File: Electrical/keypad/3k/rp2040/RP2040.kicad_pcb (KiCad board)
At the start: 4 copper layers, 66.7 x 67.2 mm, 73 parts, among them J1 Conn_01x04_Socket, P1 USB-TYPE-C-016, Q1 BSS138, SW1 TS-1187A-B-A-B, SW2 TS-1187A-B-A-B, SW3 BUTT1, SW4 BUTT2, SW5 BUTT3, U1 PRTR5V0U2X, U3 RP2040, U5 W25Q16JVSS, U6 ME6212C33M5G, U7 SLSS49E, U8 SLSS49E, U9 SLSS49E, Y1 12MHz

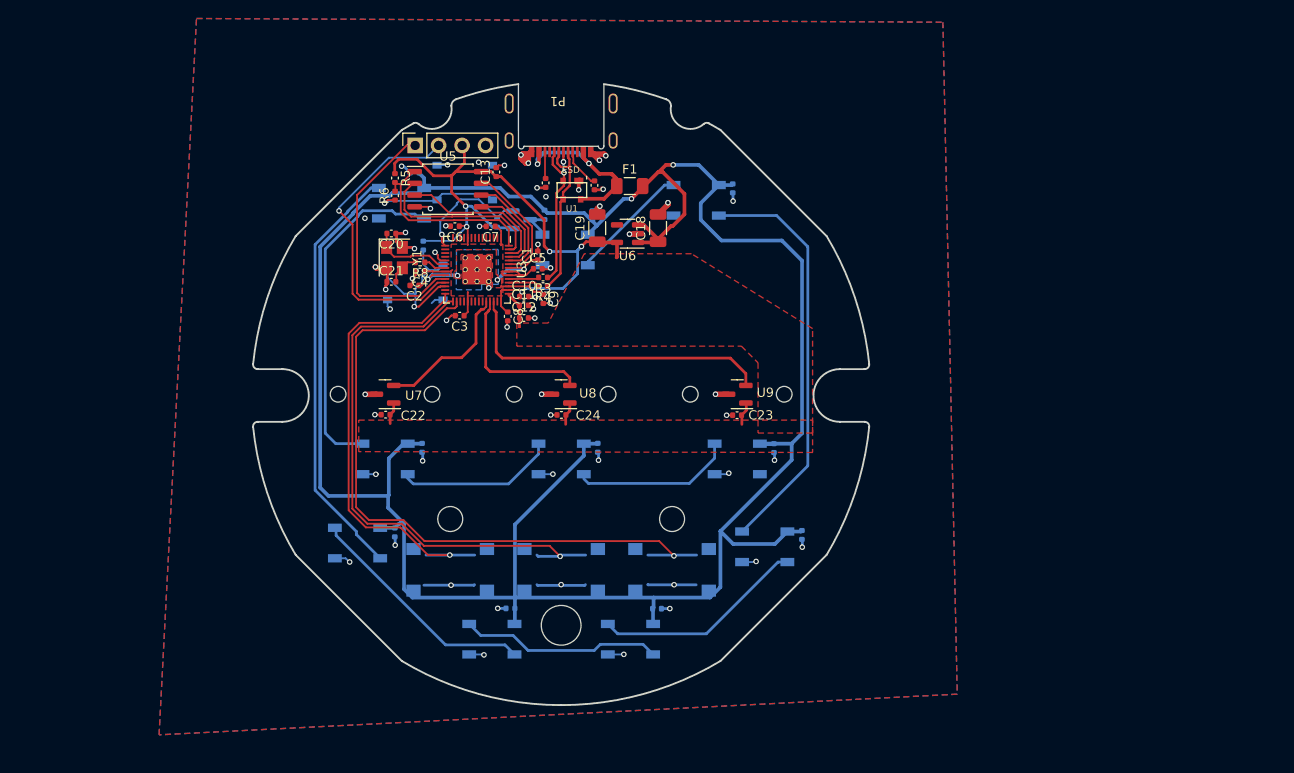
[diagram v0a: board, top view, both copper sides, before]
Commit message: adds all circuit components needed for final pcb, but may need more LED
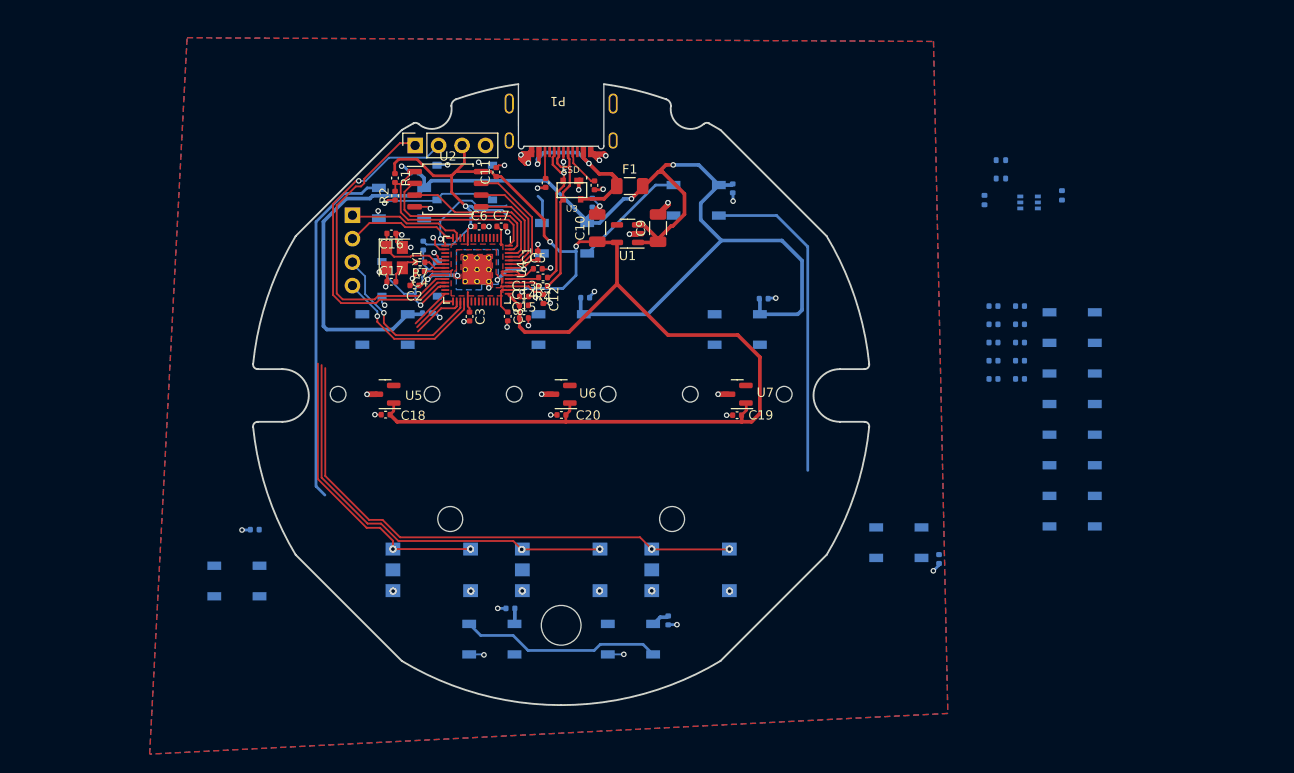
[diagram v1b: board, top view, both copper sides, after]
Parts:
- removed Q1: BSS138, Package_TO_SOT_SMD:SOT-23
- removed the SW4 at (100.0, 119.0)
- removed the SW5 at (112.0, 119.0)
- added C21: 100n, Capacitor_SMD:C_0402_1005Metric, B.Cu at (149.6, 90.5)
- added C22: 100n, Capacitor_SMD:C_0402_1005Metric, B.Cu at (149.6, 92.4)
- added C23: 100n, Capacitor_SMD:C_0402_1005Metric, B.Cu at (149.6, 94.4)
- added C31: 100n, Capacitor_SMD:C_0402_1005Metric, B.Cu at (149.6, 96.4)
- added C32: 100n, Capacitor_SMD:C_0402_1005Metric, B.Cu at (149.6, 98.3)
- added C33: 100n, Capacitor_SMD:C_0402_1005Metric, B.Cu at (146.8, 90.5)
- added C34: 100n, Capacitor_SMD:C_0402_1005Metric, B.Cu at (146.8, 92.4)
- added D10: WS2812B, LED_SMD:LED_WS2812B_PLCC4_5.0x5.0mm_P3.2mm, B.Cu at (155.3, 106.0)
- added D11: WS2812B, LED_SMD:LED_WS2812B_PLCC4_5.0x5.0mm_P3.2mm, B.Cu at (155.3, 112.7)
- added D8: WS2812B, LED_SMD:LED_WS2812B_PLCC4_5.0x5.0mm_P3.2mm, B.Cu at (155.3, 92.8)
- added D9: WS2812B, LED_SMD:LED_WS2812B_PLCC4_5.0x5.0mm_P3.2mm, B.Cu at (155.3, 99.4)
- added J1: Conn_01x04_Socket, Connector_PinSocket_2.54mm:PinSocket_1x04_P2.54mm_Vertical, B.Cu at (77.4, 80.6)
- added R10: 5.1k, Capacitor_SMD:C_0402_1005Metric, B.Cu at (146.8, 96.4)
- added R11: 5.1k, Capacitor_SMD:C_0402_1005Metric, B.Cu at (146.8, 98.3)
- added R14: 10k, Resistor_SMD:R_0402_1005Metric, B.Cu at (147.6, 74.7)
- added R15: 10k, Resistor_SMD:R_0402_1005Metric, B.Cu at (147.6, 76.7)
- added R9: 5.1k, Capacitor_SMD:C_0402_1005Metric, B.Cu at (146.8, 94.4)
- added SW1: KAN0644-0551B1-A, push_button_keypad:KAN0644, B.Cu at (86.0, 119.0)
- added SW2: KAN0644-0551B1-A, push_button_keypad:KAN0644, B.Cu at (100.0, 119.0)
- added T1: BSS138BKS_115, Package_TO_SOT_SMD:SOT-363_SC-70-6, B.Cu at (150.6, 79.2)
- SW3: value BUTT1 -> KAN0644-0551B1-A; footprint Button_Switch_SMD:SW_Push_1P1T_NO_6x6mm_H9.5mm -> push_button_keypad:KAN0644
- moved R13 56.0 mm to (154.2, 78.5)
- moved R12 52.8 mm to (145.8, 79.0)
- moved SW3 26.0 mm to (114.0, 119.0)
- moved C36 16.3 mm to (102.6, 89.6), turned to 0 degrees
- moved C37 16.2 mm to (121.9, 89.7), turned to 0 degrees
- moved C29 15.2 mm to (66.8, 114.7), turned to 180 degrees
- moved C26 15.1 mm to (140.9, 117.8)
- moved C35 14.6 mm to (85.5, 91.2), turned to 0 degrees
- moved D3 14.5 mm to (136.5, 116.1)
- moved D12 14.0 mm to (81.0, 93.0)
- moved D13 14.0 mm to (100.0, 93.0)
- moved D14 14.0 mm to (119.0, 93.0)
- moved D6 13.7 mm to (64.9, 120.2)
- moved C6 2.63 mm to (91.1, 81.9), turned to 0 degrees
- moved C27 1.75 mm to (111.6, 124.5), turned to -90 degrees
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- renumbered C19 to C10, C13 to C11, C9 to C12, C10 to C13, C11 to C14, C12 to C15, C20 to C16, C21 to C17, C22 to C18, C23 to C19, C24 to C20, C28 to C24, C29 to C25, C30 to C26, C31 to C27, C32 to C28, C33 to C29, C34 to C30, C25 to C35, C26 to C36, C27 to C37, C18 to C9, D4 to D1, D1 to D12, D2 to D13, D3 to D14, D5 to D2, D6 to D3, D7 to D4, D8 to D5, D9 to D6, D10 to D7, J1 to J2, R5 to R1, R9 to R12, R10 to R13, R6 to R2, R1 to R5, R2 to R6, R8 to R7, R7 to R8, SW1 to SW4, SW2 to SW5, U6 to U1, U5 to U2, U1 to U3, U3 to U4, U7 to U5, U8 to U6, U9 to U7
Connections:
- net LED_D renamed U_LED_D
- D12 pad 4: BL_DIN -> Net-(D12-DIN)
- D7 pad 2: BL_DIN -> Net-(D7-DOUT)
- SW3 pad 1: BUTT0 -> BUTT2
- U4 pad 13: /GPIO10 -> SDA_1
- U4 pad 14: /GPIO11 -> SCL_1
- U4 pad 16: /GPIO13 -> BL_LED_D
- U4 pad 31: /GPIO20 -> SDA_0
- U4 pad 32: /GPIO21 -> SCL_0
- U5 pad 2: ADC_IN1 -> Net-(U5-VOUT)
- U6 pad 2: ADC_IN2 -> Net-(U6-VOUT)
- U7 pad 2: ADC_IN3 -> Net-(U7-VOUT)
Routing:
- net +5V: track 260.4 -> 147.4 mm
- net +3V3: track 99.0 -> 177.0 mm
- net BL_DIN: track 36.8 -> 0.00 mm
- net ADC_IN3: track 34.8 -> 0.00 mm
- net GND: track 85.5 -> 57.7 mm, vias 59 -> 55
- net Net-(D5-DOUT): track 25.3 -> 0.00 mm
- net Net-(D3-DOUT): track 23.1 -> 0.00 mm
- net SDA_0: track 0.00 -> 18.6 mm, vias 0 -> 1
- net ADC_IN2: track 17.7 -> 0.00 mm
- net SCL_0: track 0.00 -> 17.3 mm, vias 0 -> 1
- net Net-(D13-DOUT): track 17.1 -> 0.00 mm
- net Net-(D12-DOUT): track 17.0 -> 0.00 mm
- net ADC_IN1: track 15.8 -> 0.00 mm
- net BUTT0: track 49.9 -> 37.2 mm, vias 1 -> 2
- net SDA_1: track 0.00 -> 12.6 mm
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
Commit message: reverts to using standard bs138 because the dual package one is more expensive than just using two of them, and it's easier to layout
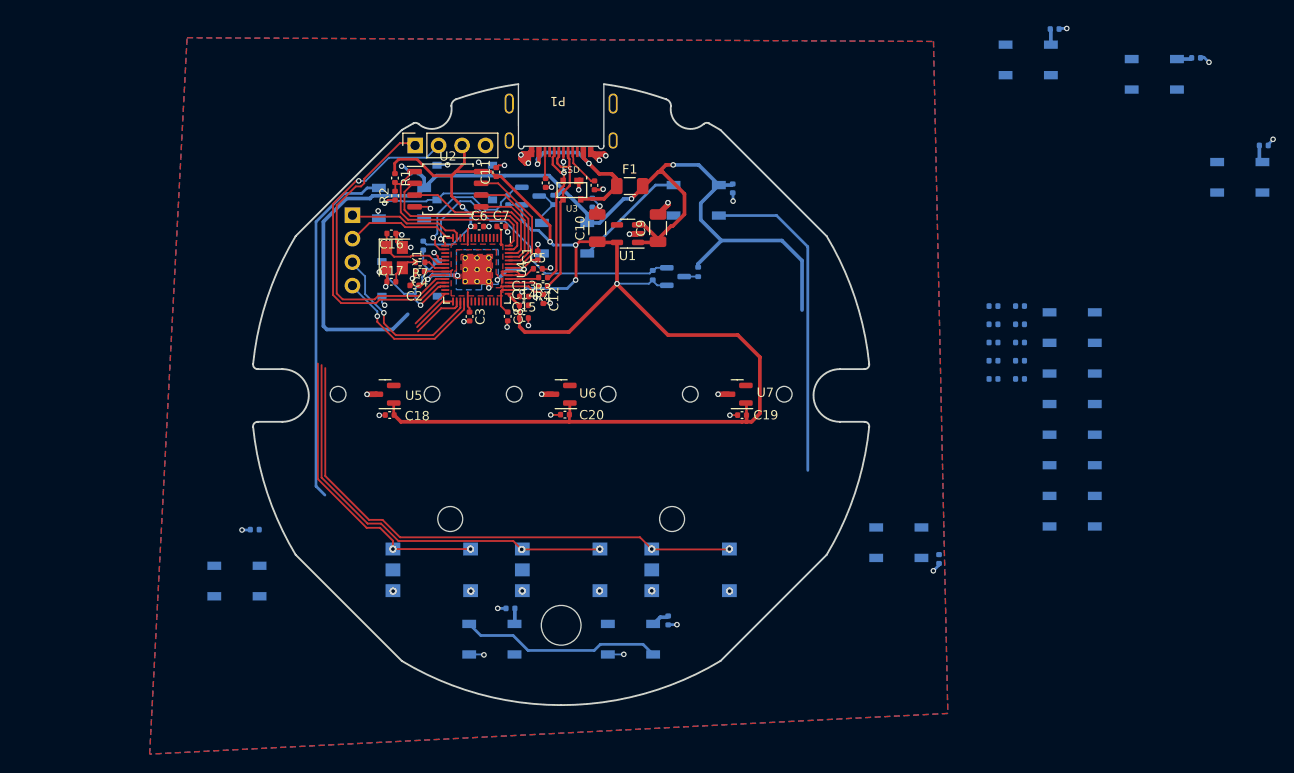
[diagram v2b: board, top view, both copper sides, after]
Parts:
- removed T1: BSS138BKS_115, Package_TO_SOT_SMD:SOT-363_SC-70-6
- added Q1: BSS138, Package_TO_SOT_SMD:SOT-23, B.Cu at (96.7, 78.6)
- added Q2: BSS138, Package_TO_SOT_SMD:SOT-23, B.Cu at (112.4, 87.3)
- moved C35 87.7 mm to (168.7, 63.6)
- moved D12 87.7 mm to (164.2, 65.4)
- moved C36 75.2 mm to (176.0, 73.1)
- moved D13 75.2 mm to (173.4, 76.5)
- moved R13 55.0 mm to (99.1, 79.0)
- moved R12 51.5 mm to (94.3, 79.0)
- moved D14 42.9 mm to (150.5, 63.8)
- moved C37 42.9 mm to (153.4, 60.5)
- moved R14 39.7 mm to (109.9, 87.1), turned to -90 degrees
- moved R15 34.3 mm to (114.8, 86.8), turned to 90 degrees
- moved C19 0.54 mm to (119.6, 102.3)
- moved C18 0.44 mm to (81.5, 102.2)
- moved C20 0.38 mm to (100.4, 102.2)
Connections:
- U4 pad 15: U_LED_D -> BL_LED_D
- U4 pad 16: BL_LED_D -> U_LED_D
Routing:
- net BL_LED_D: track 2.12 -> 32.5 mm
- net +5V: track 147.4 -> 130.7 mm
- net +3V3: track 177.0 -> 183.9 mm, vias 5 -> 7
- net U_LED_D: track 11.2 -> 16.5 mm
- net Net-(D12-DIN): track 0.00 -> 1.56 mm
- net Net-(D1-DIN): track 3.12 -> 4.57 mm

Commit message: places perkey backlight leds
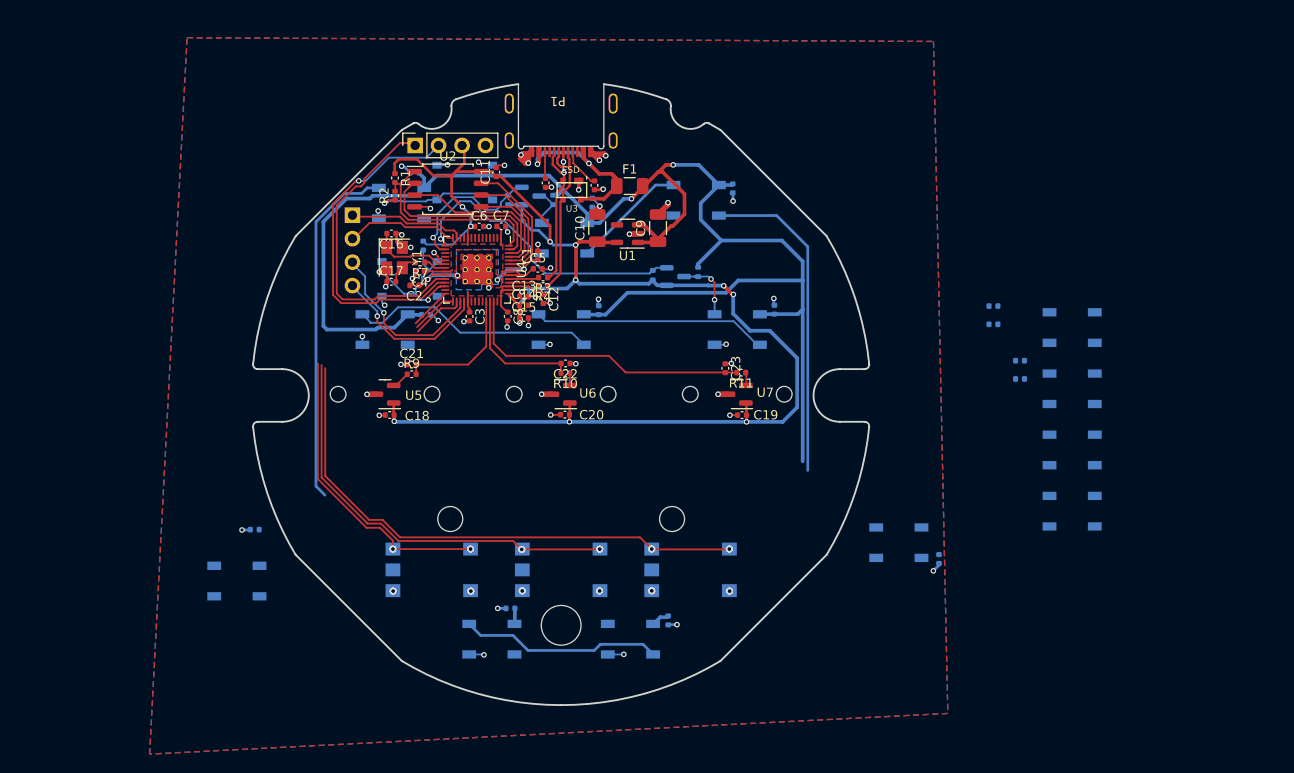
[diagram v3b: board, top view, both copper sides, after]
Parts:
- C21, C22, C23, R10, R11, R9: moved to F.Cu
- moved D14 75.4 mm to (81.0, 93.0)
- moved D13 75.2 mm to (100.0, 93.0)
- moved C37 74.7 mm to (85.4, 91.4)
- moved C36 74.1 mm to (104.1, 90.9), turned to 90 degrees
- moved C21 66.1 mm to (83.8, 96.8), turned to 0 degrees
- moved R9 63.0 mm to (83.8, 97.8), turned to 0 degrees
- moved C35 53.1 mm to (123.1, 90.8), turned to 90 degrees
- moved D12 52.9 mm to (119.0, 93.0)
- moved C22 49.3 mm to (100.5, 96.7)
- moved R10 46.3 mm to (100.5, 97.7)
- moved C23 32.0 mm to (117.8, 97.2), turned to -90 degrees
- moved R11 27.3 mm to (119.5, 97.7)
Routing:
- net +5V: track 130.7 -> 173.4 mm
- net ADC_IN3: track 0.00 -> 32.3 mm
- net Net-(D13-DOUT): track 0.00 -> 26.8 mm
- net Net-(D12-DOUT): track 0.00 -> 25.3 mm
- net ADC_IN2: track 0.00 -> 14.5 mm
- net ADC_IN1: track 0.00 -> 14.3 mm
- net Net-(D12-DIN): track 1.56 -> 7.41 mm, vias 0 -> 2
- net GND: track 57.9 -> 63.8 mm, vias 55 -> 61
- net +3V3: track 183.9 -> 178.2 mm, vias 7 -> 12
- net Net-(U5-VOUT): track 0.00 -> 1.96 mm
- net Net-(U7-VOUT): track 0.00 -> 1.44 mm
- net Net-(U6-VOUT): track 0.00 -> 1.43 mm
- net Net-(U4-RUN): track 17.6 -> 16.9 mm

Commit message: adds buttons
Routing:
- net BUTT1: track 50.5 -> 67.0 mm, vias 2 -> 3
- net BUTT2: track 64.5 -> 80.9 mm, vias 2 -> 3
- net BUTT0: track 37.2 -> 53.5 mm, vias 2 -> 3

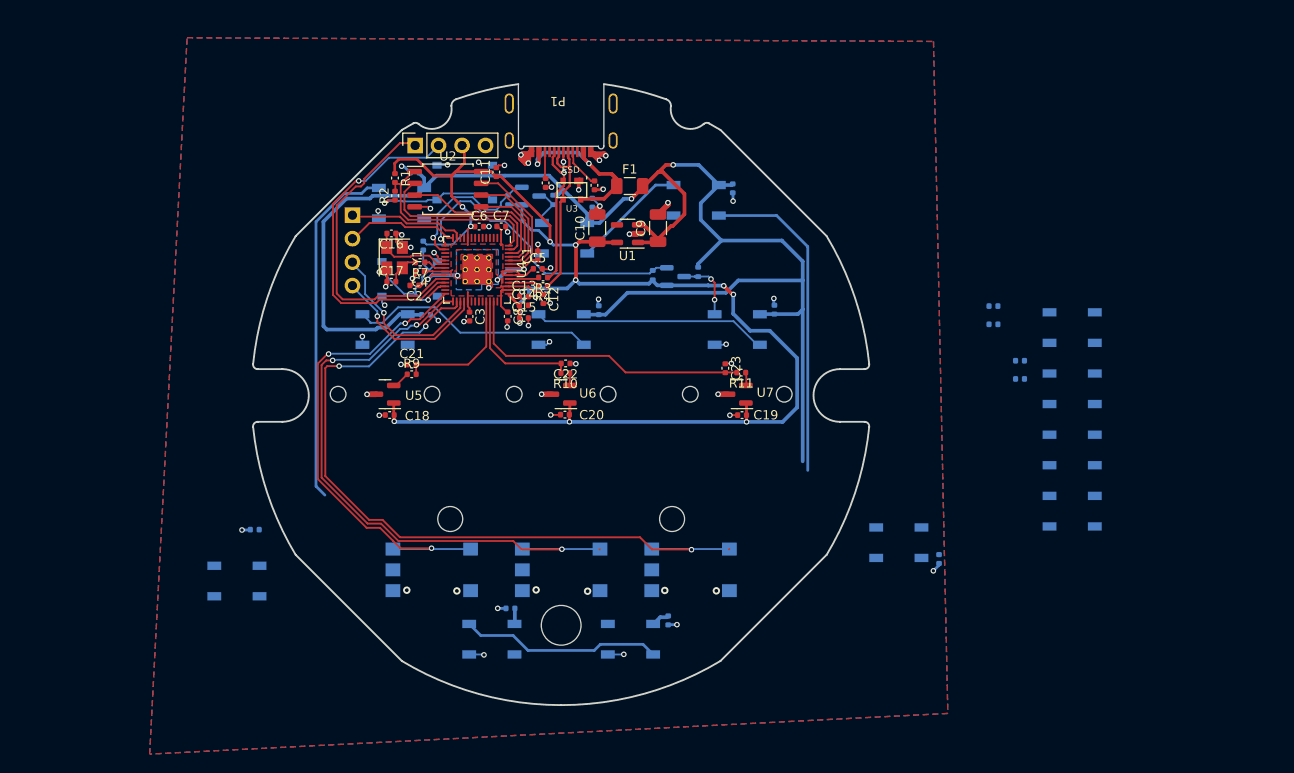
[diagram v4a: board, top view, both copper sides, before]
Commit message: adds 2020 led to smoothen out LED diffusing on sides
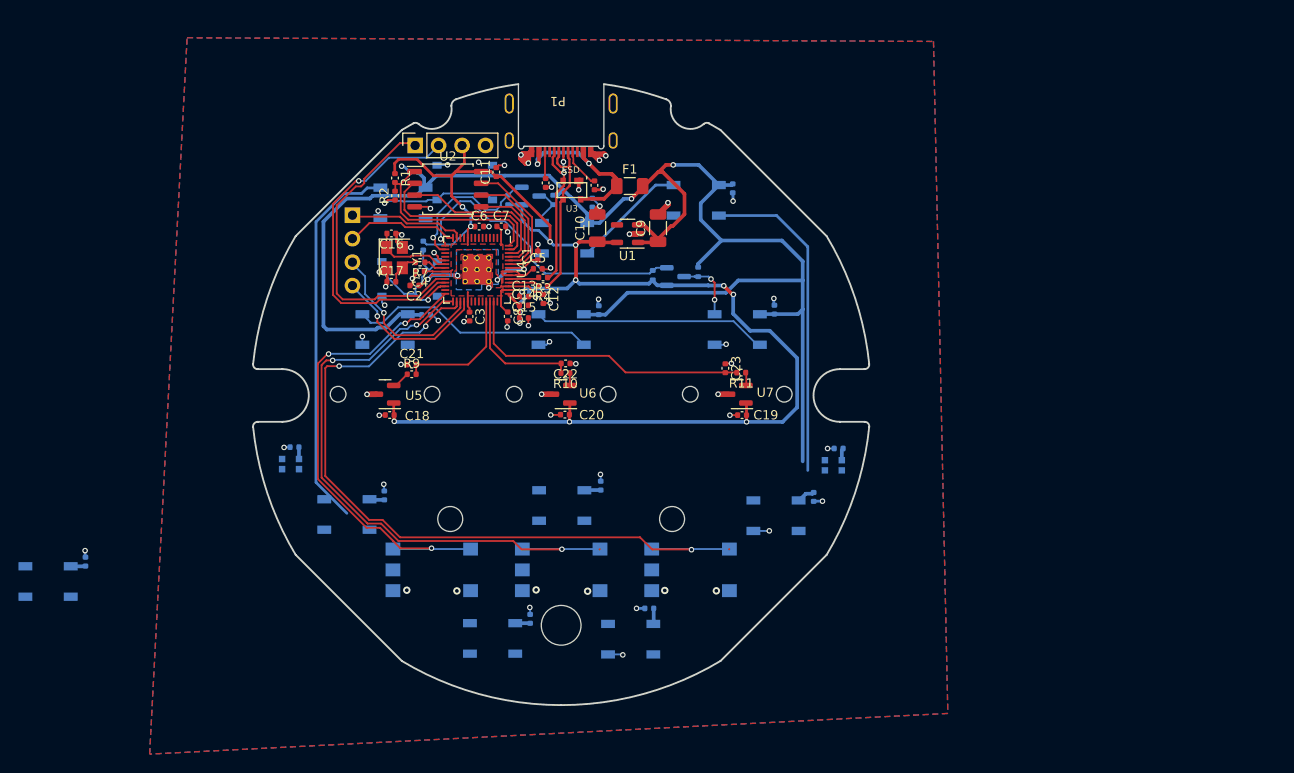
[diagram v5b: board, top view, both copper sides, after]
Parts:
- D10, D3: value WS2812B -> WS2812-2020; footprint LED_SMD:LED_WS2812B_PLCC4_5.0x5.0mm_P3.2mm -> footprints:LED_WS2812-2020
- moved D9 112.7 mm to (44.5, 120.3)
- moved D10 84.6 mm to (70.7, 107.6), turned to 0 degrees
- moved D8 81.0 mm to (76.8, 113.0)
- moved D11 79.7 mm to (82.9, 79.3)
- moved C33 77.1 mm to (71.2, 105.7)
- moved C31 70.3 mm to (80.9, 111.0), turned to 90 degrees
- moved C34 64.8 mm to (84.1, 76.0)
- moved C30 49.9 mm to (96.6, 124.3), turned to 90 degrees
- moved D7 48.1 mm to (92.6, 126.4)
- moved C32 46.8 mm to (104.3, 109.9), turned to 90 degrees
- moved D6 36.1 mm to (100.1, 112.0)
- moved C27 20.6 mm to (127.3, 111.1)
- moved D4 20.6 mm to (123.2, 113.1)
- moved C29 18.6 mm to (48.5, 118.1), turned to 90 degrees
- moved C26 16.2 mm to (130.0, 105.9), turned to 180 degrees
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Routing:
- net Net-(D10-DO): track 0.00 -> 41.2 mm
- net Net-(D6-DOUT): track 38.3 -> 0.00 mm
- net Net-(D4-DOUT): track 21.8 -> 0.00 mm
- net +5V: track 173.4 -> 182.0 mm
- net GND: track 63.8 -> 66.7 mm, vias 61 -> 65
